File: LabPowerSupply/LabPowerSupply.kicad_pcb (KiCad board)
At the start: 2 copper layers, 222 parts, among them Q1_LVR1 PJA3404_R1_00001, Q1_LVR2 PJA3404_R1_00001, Q2_LVR1 PJA3404_R1_00001, Q2_LVR2 PJA3404_R1_00001, Q3_LVR1 PJA3404_R1_00001, Q3_LVR2 PJA3404_R1_00001, SW11 Decimal, SW12 0, SW13 Backspace, SW14 Current 2, SW15 Cancel, SW21 1, SW22 2, SW23 3, SW24 Voltage 2, SW25 Confirm, SW31 4, SW32 5, SW33 6, SW34 Current 1, SW35 Channel 2, SW41 7, SW42 8, SW43 9, SW44 Voltage 1, SW45 Channel 1, Y1 8M, Y2 8M

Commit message: Pre regulate 3.3v
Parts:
- added C1_5V2: 68u, Capacitor_THT:CP_Radial_D8.0mm_P3.50mm, F.Cu at (226.1, -30.5)
- added C2_5V2: 100n, Capacitor_SMD:C_0603_1608Metric, F.Cu at (234.6, -34.0)
- added C3_5V2: 68u, Capacitor_THT:CP_Radial_D8.0mm_P3.50mm, F.Cu at (216.3, -30.5)
- added L_5V2: 4.7u, Inductor_SMD:L_Sumida_CDMC6D28_7.25x6.5mm, F.Cu at (217.7, -21.7)
- added U_5V2: AP63205WU, Package_TO_SOT_SMD:TSOT-23-6, F.Cu at (224.9, -23.5)
- moved FrontPanel1 271.5 mm to (-84.6, -72.4)
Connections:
- C1_3.3V1 pad 2: VCC -> /Channel 1 Power Rails/5 Volts
- C1_3.3V2 pad 2: VDD -> Net-(C3_5V2-Pad1)
- U_3.3V1 pad 3: VCC -> /Channel 1 Power Rails/5 Volts
- U_3.3V2 pad 3: VDD -> Net-(C3_5V2-Pad1)
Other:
- copper layers 2 -> 4

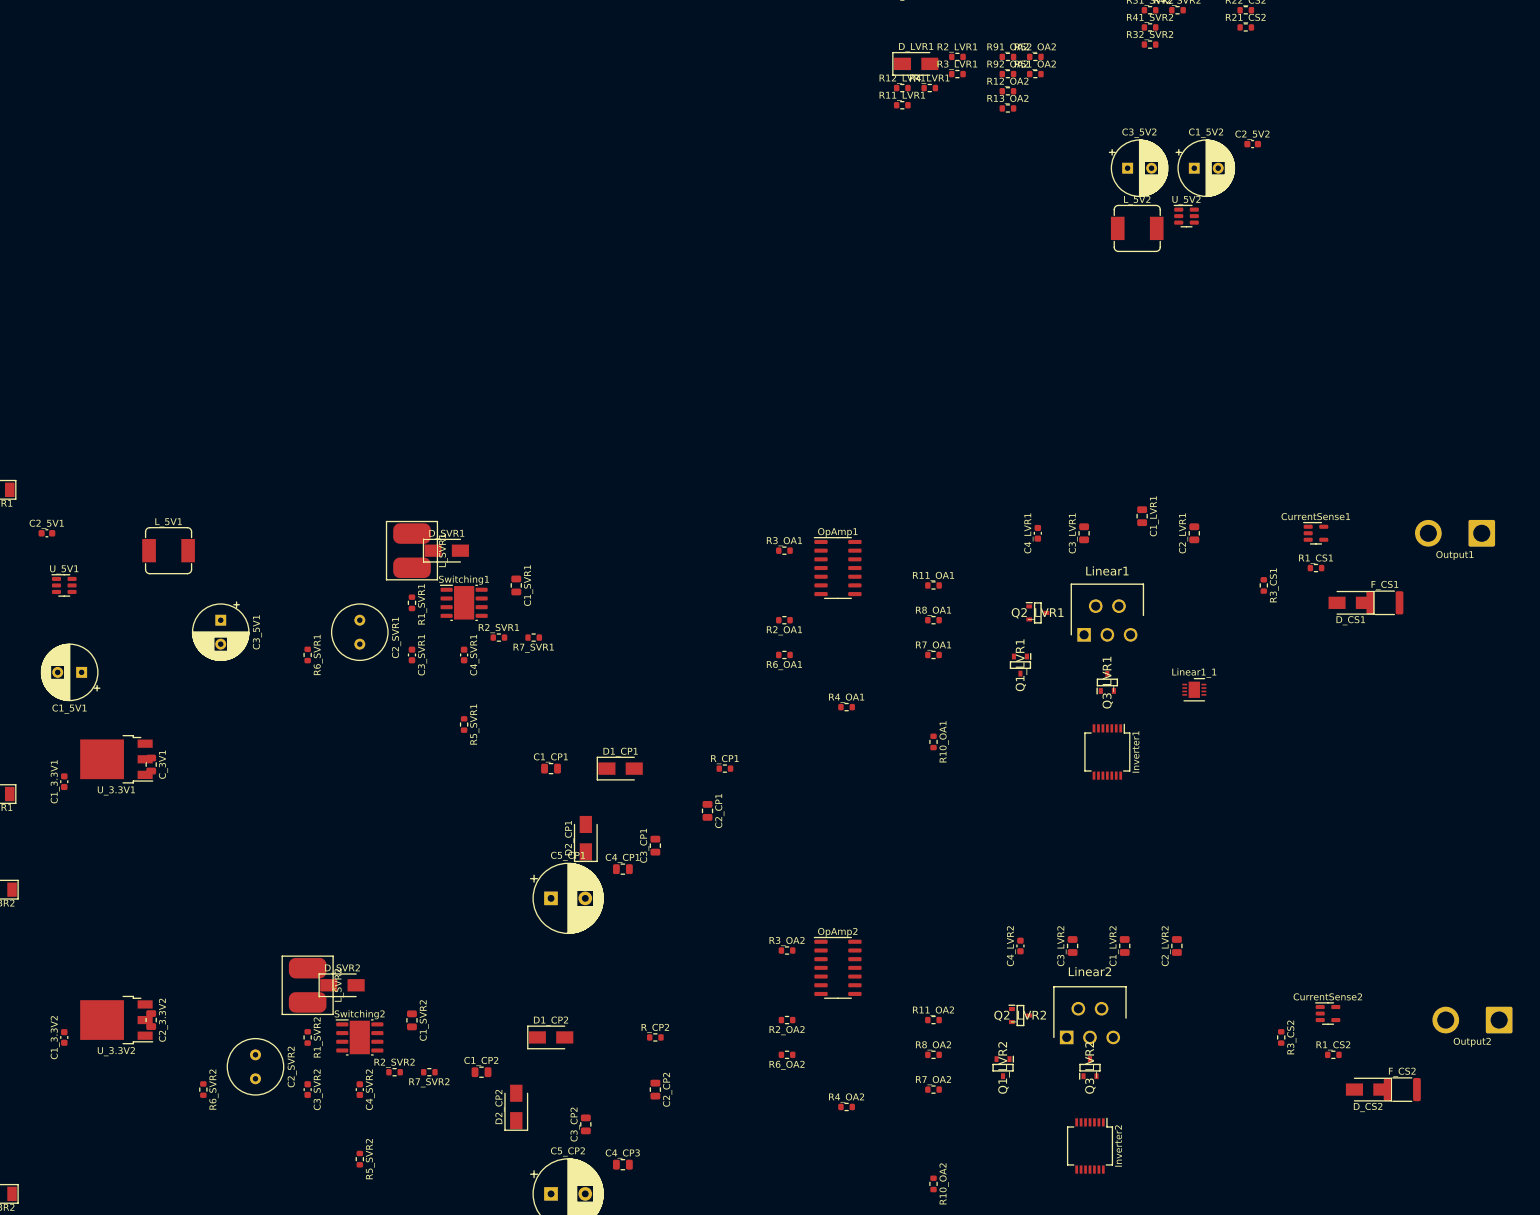
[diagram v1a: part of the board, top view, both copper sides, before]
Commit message: Changed capacitors to x7r
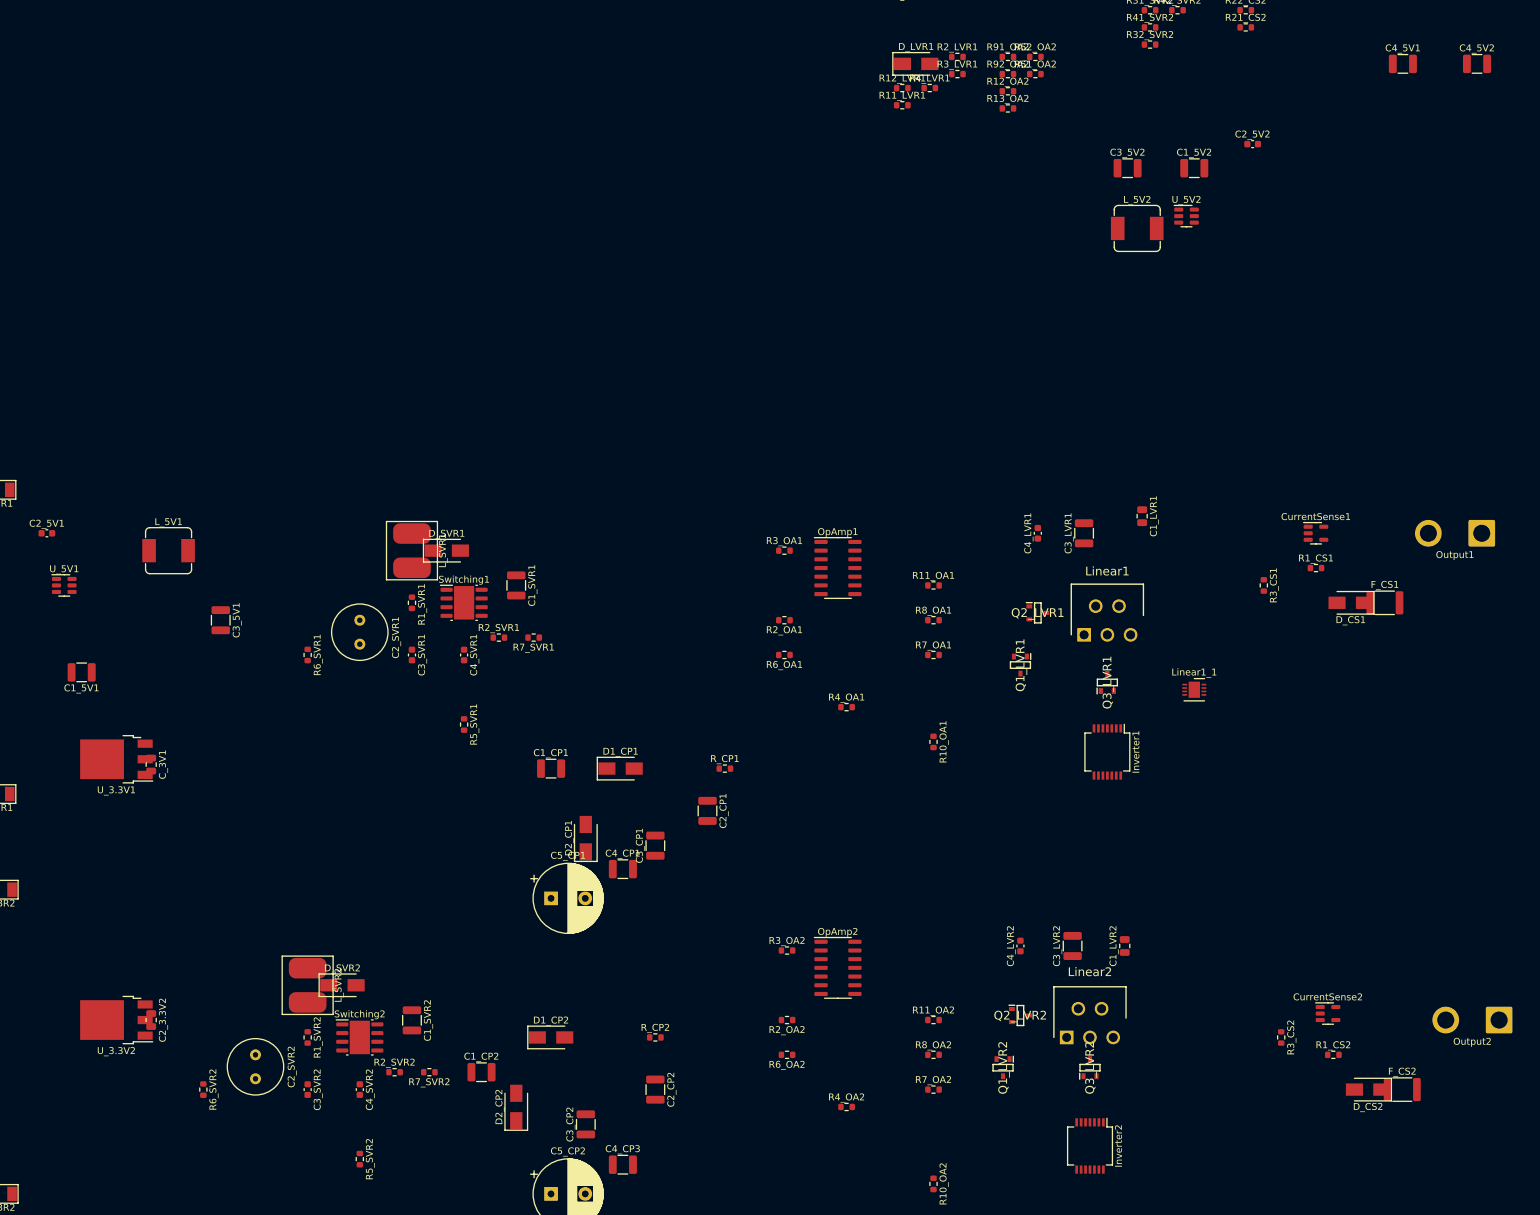
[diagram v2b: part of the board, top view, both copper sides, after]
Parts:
- removed C1_3.3V1, C1_3.3V2: 1u, Capacitor_SMD:C_0603_1608Metric
- removed C2_LVR1, C2_LVR2: 10u, Capacitor_SMD:C_0805_2012Metric
- added C4_5V1: 22u, Capacitor_SMD:C_1210_3225Metric, F.Cu at (256.5, -45.7)
- added C4_5V2: 22u, Capacitor_SMD:C_1210_3225Metric, F.Cu at (267.4, -45.7)
- C1_5V1, C1_5V2: value 68u -> 10u; footprint Capacitor_THT:CP_Radial_D8.0mm_P3.50mm -> Capacitor_SMD:C_1210_3225Metric
- C1_CP1, C1_CP2, C1_SVR1, C1_SVR2, C2_CP1, C2_CP2, C3_CP1, C3_CP2, C3_LVR1, C3_LVR2, C4_CP1, C4_CP3: footprint Capacitor_SMD:C_0805_2012Metric -> Capacitor_SMD:C_1210_3225Metric
- C3_5V1, C3_5V2: value 68u -> 22u; footprint Capacitor_THT:CP_Radial_D8.0mm_P3.50mm -> Capacitor_SMD:C_1210_3225Metric
- C4_LVR1, C4_LVR2: value 100n -> 20p
- R2_LVR1, R2_LVR2: value 0 -> 1k
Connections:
- C1_5V1 pad 1: VCC -> GND1
- C1_5V1 pad 2: GND1 -> VCC
- C1_5V2 pad 1: VDD -> GND2
- C1_5V2 pad 2: GND2 -> VDD
- C3_5V1 pad 1: /Channel 1 Power Rails/5 Volts -> GND1
- C3_5V1 pad 2: GND1 -> /Channel 1 Power Rails/5 Volts
- C3_5V2 pad 1: Net-(C3_5V2-Pad1) -> GND2
- C3_5V2 pad 2: GND2 -> Net-(C3_5V2-Pad2)
- L_5V2 pad 2: Net-(C3_5V2-Pad1) -> Net-(C3_5V2-Pad2)
- U_3.3V2 pad 3: Net-(C3_5V2-Pad1) -> Net-(C3_5V2-Pad2)
- U_5V2 pad 1: Net-(C3_5V2-Pad1) -> Net-(C3_5V2-Pad2)

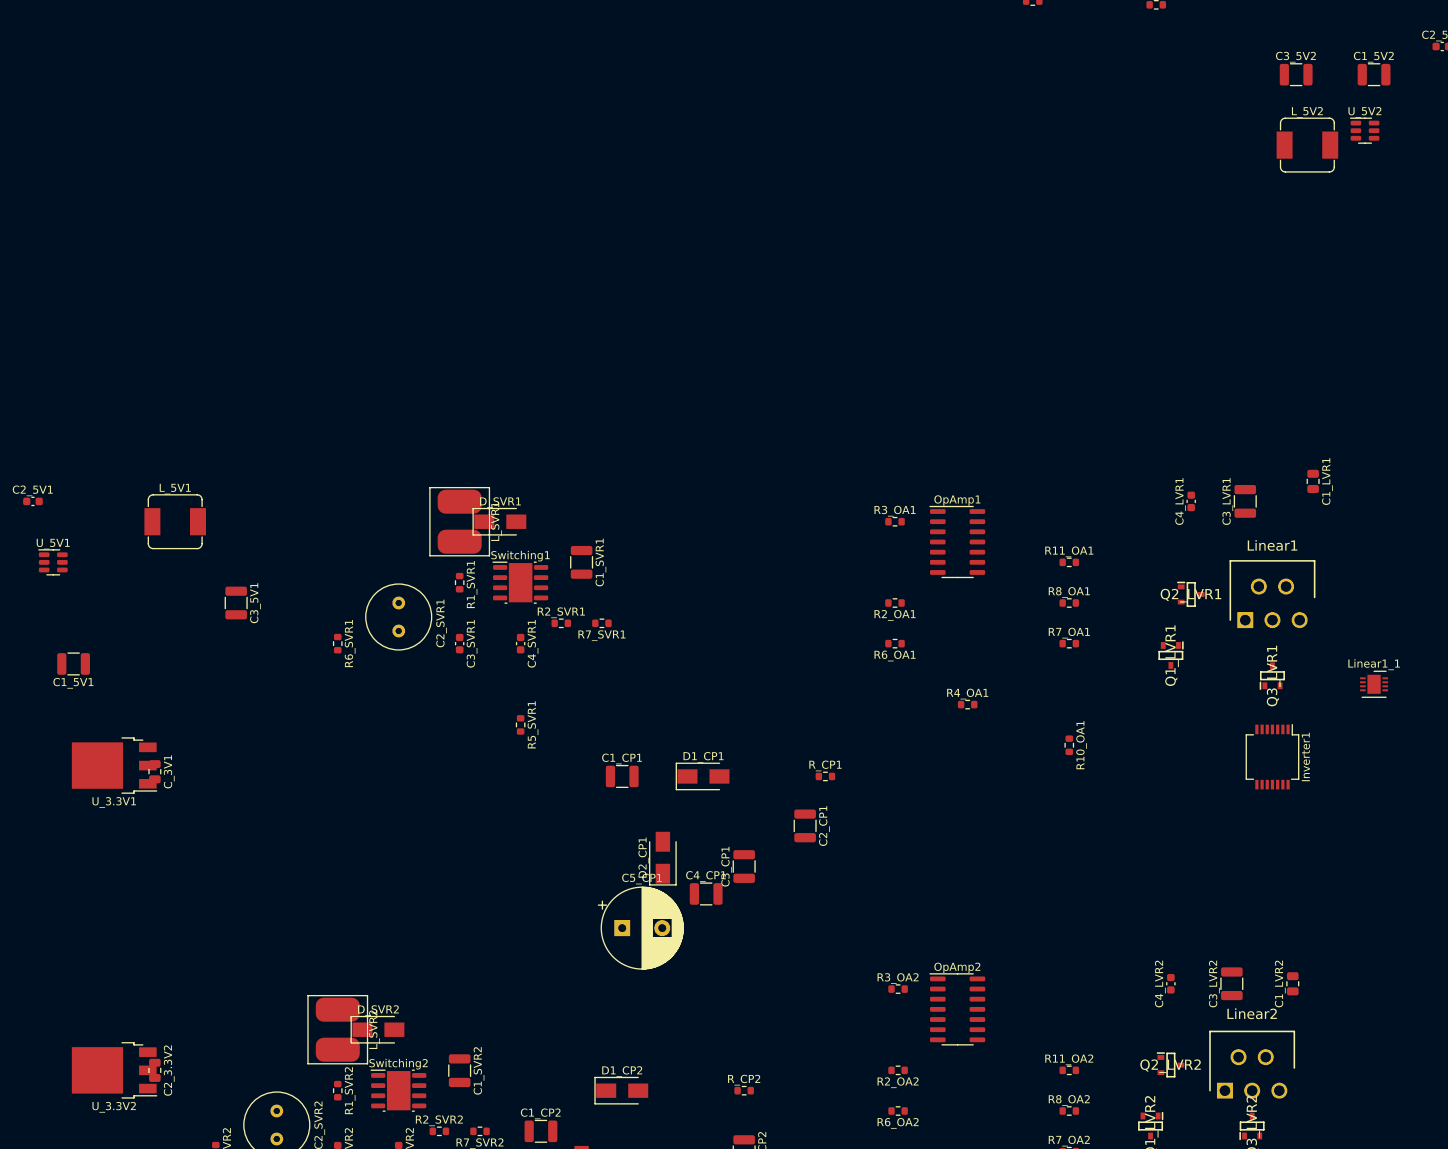
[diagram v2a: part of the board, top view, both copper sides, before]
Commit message: Fixed cap footprints
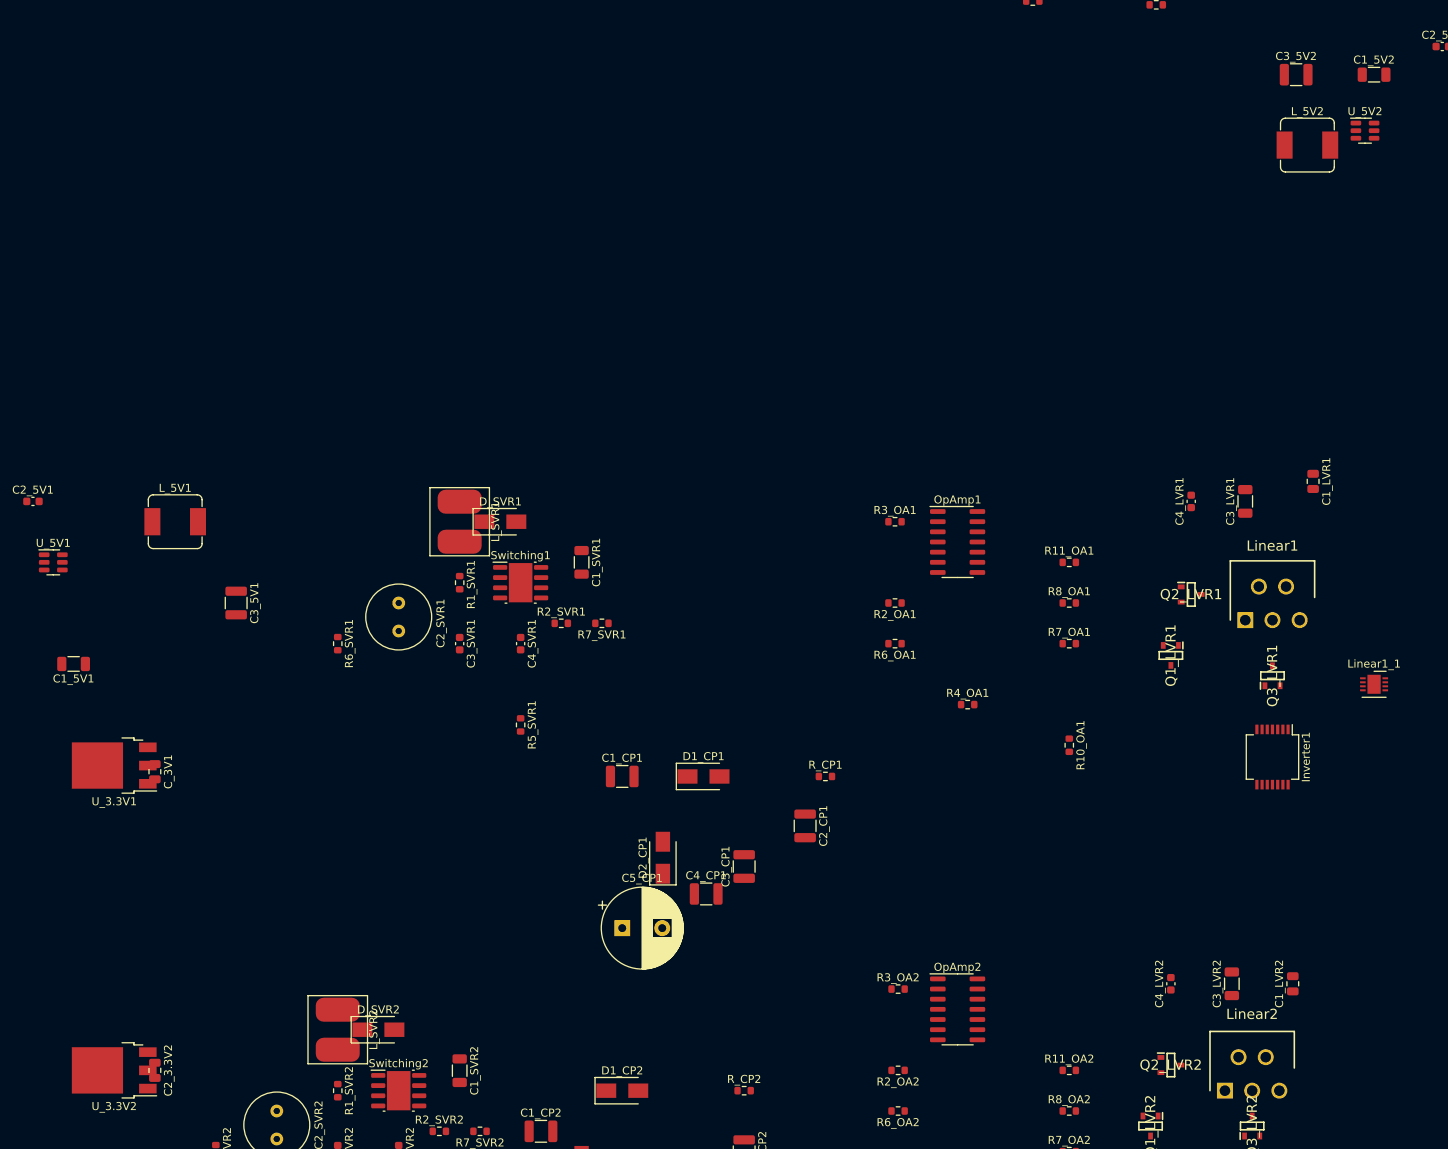
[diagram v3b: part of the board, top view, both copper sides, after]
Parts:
- C1_5V1, C1_5V2, C1_SVR1, C1_SVR2, C3_LVR1, C3_LVR2: footprint Capacitor_SMD:C_1210_3225Metric -> Capacitor_SMD:C_1206_3216Metric

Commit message: SMD Oscillator
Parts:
- added Q1_CP1: FMMT495TA, Package_TO_SOT_SMD:SOT-23, F.Cu at (254.0, -63.5)
- added Q1_CP2: FMMT495TA, Package_TO_SOT_SMD:SOT-23, F.Cu at (265.9, -63.5)
- Y1, Y2: footprint Crystal:Crystal_HC18-U_Vertical -> Crystal:Crystal_SMD_HC49-SD
- moved C1_LVR1 31.3 mm to (232.6, 48.3), turned to 180 degrees
- moved C4_LVR1 28.7 mm to (230.1, 33.0), turned to 0 degrees
- moved C3_LVR1 26.3 mm to (230.1, 39.8), turned to 0 degrees
- moved Inverter1 19.2 mm to (198.1, 43.2), turned to 180 degrees
- moved Linear1_1 15.5 mm to (241.3, 48.3)
- moved Q1_LVR1 15.4 mm to (210.8, 30.5), turned to 180 degrees
- moved Q2_LVR1 15.3 mm to (218.4, 33.0), turned to -90 degrees
- moved Linear1 5.67 mm to (215.2, 39.8), turned to -90 degrees
- moved Q3_LVR1 5.29 mm to (208.3, 43.2), turned to 0 degrees
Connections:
- R_CP1 pad 2: unconnected-(R_CP1-Pad2) -> Net-(R_CP1-Pad2)
- R_CP2 pad 2: unconnected-(R_CP2-Pad2) -> Net-(R_CP2-Pad2)

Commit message: removed transformer and bug squached
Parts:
- removed FrontPanel1: Conn_02x10_Counter_Clockwise, Connector_IDC:IDC-Header_2x10_P2.54mm_Vertical
- removed Mains1: Conn_01x02, Connector_TE-Connectivity:TE_MATE-N-LOK_1-770866-x_1x02_P4.14mm_Vertical
- removed Transformer1: FS24-800-C2, SamacSys_Parts:FS24800C2
- added Front_Panel2: Conn_02x08_Counter_Clockwise, Connector_IDC:IDC-Header_2x08_P2.54mm_Vertical, F.Cu at (-75.7, -74.9)
- added Input1: Conn_01x01, Connector_Wire:SolderWire-2sqmm_1x01_D2mm_OD3.9mm, F.Cu at (24.1, 61.0)
- added Input2: Conn_01x01, Connector_Wire:SolderWire-2sqmm_1x01_D2mm_OD3.9mm, F.Cu at (24.1, 16.5)
- added Input3: Conn_01x01, Connector_Wire:SolderWire-2sqmm_1x01_D2mm_OD3.9mm, F.Cu at (23.8, 113.0)
- added Input4: Conn_01x01, Connector_Wire:SolderWire-2sqmm_1x01_D2mm_OD3.9mm, F.Cu at (23.8, 68.6)
- Front_Panel1: value Conn_02x10_Counter_Clockwise -> Conn_02x08_Counter_Clockwise; footprint Connector_IDC:IDC-Header_2x10_P2.54mm_Vertical -> Connector_IDC:IDC-Header_2x08_P2.54mm_Vertical
- J_I2C1: value Conn_01x03_Male -> Conn_01x04_Male; footprint Connector_PinHeader_2.54mm:PinHeader_1x03_P2.54mm_Vertical -> Connector_PinHeader_2.54mm:PinHeader_1x04_P2.54mm_Vertical
- J_STLink1, J_STLink2: value Conn_01x03_Male -> Conn_01x05_Male; footprint Connector_PinHeader_2.54mm:PinHeader_1x03_P2.54mm_Vertical -> Connector_PinHeader_2.54mm:PinHeader_1x05_P2.54mm_Vertical
- moved D2_BR2 22.2 mm to (29.8, 113.0)
- moved D4_BR2 22.2 mm to (29.8, 68.6)
- moved D3_BR2 20.4 mm to (17.8, 68.6)
- moved D1_BR2 20.4 mm to (17.8, 113.0)
- moved D2_BR1 20.3 mm to (30.5, 61.0)
- moved D4_BR1 20.3 mm to (30.5, 16.5)
- moved D1_BR1 19.0 mm to (17.8, 61.0)
- moved D3_BR1 19.0 mm to (17.8, 16.5)
- moved C1_BR2 16.8 mm to (27.6, 100.3)
- moved C2_BR2 16.8 mm to (27.6, 81.3)
- moved C1_BR1 15.6 mm to (27.6, 48.3)
- moved C2_BR1 15.6 mm to (27.6, 29.2)

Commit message: Changed grid size, began regrouping
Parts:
- removed C2_3.3V2: 2.2u, Capacitor_SMD:C_0805_2012Metric
- added C_3.3V2: 2.2u, Capacitor_SMD:C_0805_2012Metric, F.Cu at (68.6, 130.5)
- OpAmp1, OpAmp2, R10_OA1, R10_OA2, R11_OA1, R11_OA2, R12_OA1, R12_OA2, R13_OA1, R13_OA2, R2_OA1, R2_OA2, R2_SVR1, R2_SVR2, R31_SVR1, R31_SVR2, R32_SVR1, R32_SVR2, R3_OA1, R3_OA2, R41_SVR1, R41_SVR2, R42_SVR1, R42_SVR2, R4_OA1, R4_OA2, R51_OA1, R51_OA2, R52_OA1, R52_OA2, R6_OA1, R6_OA2, R6_SVR1, R6_SVR2, R7_OA1, R7_OA2, R7_SVR1, R7_SVR2, R8_OA1, R8_OA2, R91_OA1, R91_OA2, R92_OA1, R92_OA2: moved to B.Cu
- moved C4_5V2 282.9 mm to (56.9, 143.2)
- moved Q1_CP2 243.4 mm to (91.4, 106.2), turned to -90 degrees
- moved C1_5V2 242.5 mm to (50.3, 136.6), turned to 180 degrees
- moved C2_5V2 242.2 mm to (56.9, 130.5), turned to 90 degrees
- moved U_5V2 233.5 mm to (50.0, 131.2)
- moved C4_5V1 232.0 mm to (57.4, 73.3)
- moved C3_5V2 231.3 mm to (56.9, 137.1)
- moved L_5V2 221.4 mm to (50.0, 122.9), turned to 180 degrees
- moved R42_SVR2 212.4 mm to (98.2, 117.9)
- moved R31_SVR2 209.9 mm to (105.2, 122.4)
- moved R41_SVR2 204.9 mm to (102.1, 116.8), turned to 90 degrees
- moved R32_SVR2 202.7 mm to (109.2, 121.4), turned to 90 degrees
- moved Q1_CP1 190.1 mm to (90.9, 34.2), turned to -90 degrees
- moved R42_SVR1 186.4 mm to (96.5, 45.7)
- moved R31_SVR1 182.5 mm to (103.6, 50.3)
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
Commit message: Finished grouping regulation parts
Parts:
- C10_Power1, C1_Power1, C1_Power2, C1_Y1, C1_Y2, C2_Power1, C2_Power2, C2_Y1, C2_Y2, C3_Power1, C3_Power2, C4_Power1, C4_Power2, C5_Power1, C5_Power2, C6_Power1, C6_Power2, C7_Power1, C7_Power2, C8_Power1, C8_Power2, C9_Power1, CurrentSense1, CurrentSense2, Inverter1, Inverter2, MCU_1, MCU_2, Optocoupler1, Optocoupler2, Q1_LVR1, Q1_LVR2, Q2_LVR1, Q2_LVR2, Q3_LVR1, Q3_LVR2, R1_Boot1, R1_Boot2, R21_CS1, R21_CS2, R22_CS1, R22_CS2, R2_Boot1, R2_Boot2, R2_LVR1, R2_LVR2, R3_CS1, R3_CS2, R3_LVR1, R3_LVR2, R4_LVR1, R4_LVR2, R_Reset1, R_Reset2, SW_Reset1, SW_Reset2, Y1, Y2: moved to B.Cu
- moved R1_LED2 247.4 mm to (-64.0, -58.9), turned to 90 degrees
- moved R4_LVR2 223.2 mm to (185.9, 131.1), turned to -90 degrees
- moved D_LVR2 221.2 mm to (182.8, 116.3)
- moved R21_CS2 215.4 mm to (141.2, 143.6), turned to 90 degrees
- moved R2_LVR2 212.7 mm to (158.5, 104.6), turned to 180 degrees
- moved R12_LVR2 212.3 mm to (175.3, 99.6), turned to 180 degrees
- moved R22_CS2 211.7 mm to (141.2, 137.0), turned to 90 degrees
- moved R3_LVR2 210.5 mm to (174.2, 108.2), turned to -90 degrees
- moved R11_LVR2 210.2 mm to (168.1, 99.6), turned to 180 degrees
- moved Linear1_2 192.6 mm to (184.9, 91.4)
- moved R21_CS1 190.5 mm to (133.6, 64.5), turned to 90 degrees
- moved R22_CS1 187.3 mm to (133.6, 57.9), turned to 90 degrees
- moved Output1 126.6 mm to (147.8, 62.5), turned to -90 degrees
- moved Output2 124.6 mm to (155.4, 141.6), turned to -90 degrees
- moved R1_CS1 124.5 mm to (126.0, 68.1), turned to 180 degrees
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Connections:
- D_LVR1 pad 2: Net-(D_LVR1-Pad2) -> /Channel Power Supply 1/Charge Pump/Charge
- D_LVR2 pad 2: Net-(D_LVR2-Pad2) -> /Channel Power Supply 2/Charge Pump/Charge
- Q3_LVR1 pad 3: Net-(D_LVR1-Pad2) -> /Channel Power Supply 1/Charge Pump/Charge
- Q3_LVR2 pad 3: Net-(D_LVR2-Pad2) -> /Channel Power Supply 2/Charge Pump/Charge
